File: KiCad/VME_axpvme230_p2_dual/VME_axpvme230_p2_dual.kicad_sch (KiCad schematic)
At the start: 16 parts, among them J1 DIN41612_03x32_ABC, J2 DIN41612_03x32_ABC, J3 SCSI BUS

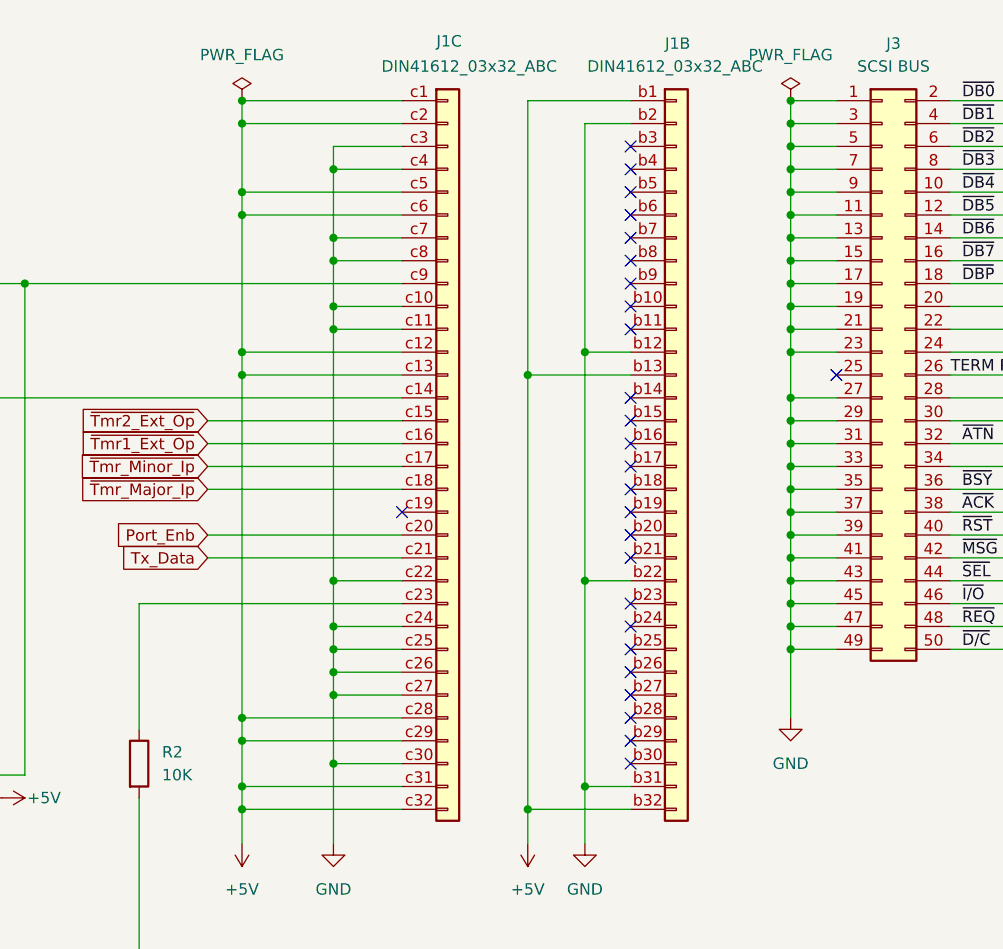
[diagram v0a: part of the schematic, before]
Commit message: R2を2KΩに変更
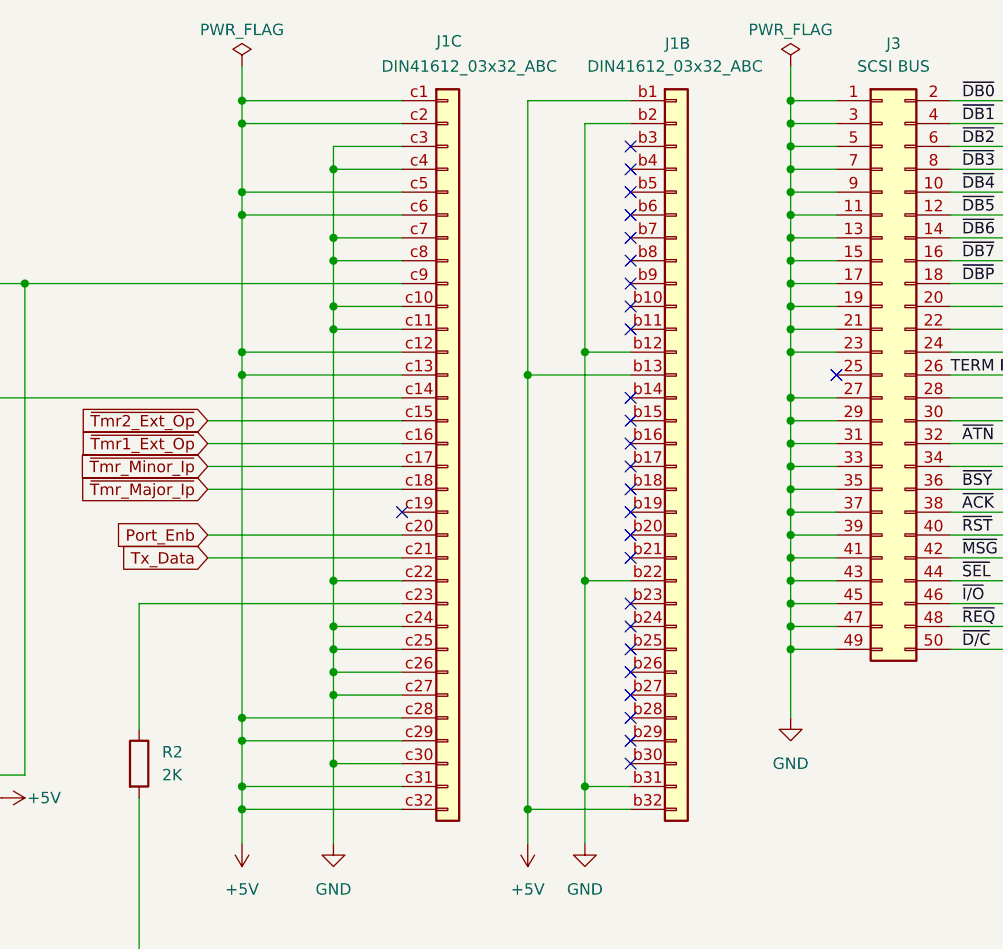
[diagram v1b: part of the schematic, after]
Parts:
- R2: value 10K -> 2K
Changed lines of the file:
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@@
 	(title_block
 		(title "AXPvme Double-Slot Breakout Module")
-		(date "2026-07-11")
-		(rev "0.1")
+		(date "2026-07-28")
+		(rev "0.2")
 		(company "kanpapa.com")
 		(comment 1 "for DEC AXPVME230")
@@
 	)
 	(junction
+		(at 64.77 25.4)
+		(diameter 0)
+		(color 0 0 0 0)
+	)
+	(junction
 		(at 125.73 33.02)
 		(diameter 0)
@@
 	)
 	(junction
+		(at 125.73 25.4)
+		(diameter 0)
+		(color 0 0 0 0)
+	)
+	(junction
 		(at 207.01 96.52)
 		(diameter 0)
@@
 	)
 	(junction
-		(at 64.77 25.4)
-		(diameter 0)
-		(color 0 0 0 0)
-	)
-	(junction
 		(at 64.77 93.98)
 		(diameter 0)
@@
 	)
 	(junction
-		(at 125.73 25.4)
-		(diameter 0)
-		(color 0 0 0 0)
-	)
-	(junction
 		(at 125.73 48.26)
 		(diameter 0)
@@
 	(wire
 		(pts
+			(xy 64.77 21.59) (xy 64.77 25.4)
+		)
+		(stroke
+			(width 0)
+			(type default)
+		)
+	)
+	(wire
+		(pts
 			(xy 125.73 71.12) (xy 130.81 71.12)
 		)
@@
 	(wire
 		(pts
+			(xy 125.73 21.59) (xy 125.73 25.4)
+		)
+		(stroke
+			(width 0)
+			(type default)
+		)
+	)
+	(wire
+		(pts
 			(xy 74.93 50.8) (xy 82.55 50.8)
 		)
@@
 			)
 		)
-		(property "Value" "10K"
+		(property "Value" "2K"
 			(at 55.88 100.3299 0)
 			(show_name no)
@@
 	(symbol
 		(lib_id "power:PWR_FLAG")
-		(at 64.77 25.4 0)
+		(at 64.77 21.59 0)
 		(unit 1)
 		(body_style 1)
@@
 		(in_pos_files yes)
 		(dnp no)
-		(fields_autoplaced yes)
 		(property "Reference" "#FLG04"
-			(at 64.77 23.495 0)
+			(at 64.77 19.685 0)
 			(hide yes)
 			(show_name no)
@@
 		)
 		(property "Value" "PWR_FLAG"
-			(at 64.77 20.32 0)
+			(at 64.77 17.526 0)
 			(show_name no)
 			(do_not_autoplace no)
@@
 		)
 		(property "Footprint" ""
-			(at 64.77 25.4 0)
+			(at 64.77 21.59 0)
 			(hide yes)
 			(show_name no)
@@
 		)
 		(property "Datasheet" ""
-			(at 64.77 25.4 0)
+			(at 64.77 21.59 0)
 			(hide yes)
 			(show_name no)
@@
 		)
 		(property "Description" ""
-			(at 64.77 25.4 0)
+			(at 64.77 21.59 0)
 			(show_name no)
 			(do_not_autoplace no)
@@
 	(symbol
 		(lib_id "power:PWR_FLAG")
-		(at 125.73 25.4 0)
+		(at 125.73 21.59 0)
 		(unit 1)
 		(body_style 1)
@@
 		(in_pos_files yes)
 		(dnp no)
-		(fields_autoplaced yes)
 		(property "Reference" "#FLG05"
-			(at 125.73 23.495 0)
+			(at 125.73 19.685 0)
 			(hide yes)
 			(show_name no)
@@
 		)
 		(property "Value" "PWR_FLAG"
-			(at 125.73 20.32 0)
+			(at 125.73 17.526 0)
 			(show_name no)
 			(do_not_autoplace no)
@@
 		)
 		(property "Footprint" ""
-			(at 125.73 25.4 0)
+			(at 125.73 21.59 0)
 			(hide yes)
 			(show_name no)
@@
 		)
 		(property "Datasheet" ""
-			(at 125.73 25.4 0)
+			(at 125.73 21.59 0)
 			(hide yes)
 			(show_name no)
@@
 		)
 		(property "Description" ""
-			(at 125.73 25.4 0)
+			(at 125.73 21.59 0)
 			(show_name no)
 			(do_not_autoplace no)
